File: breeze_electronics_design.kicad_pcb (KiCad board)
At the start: 2 copper layers, 104.1 x 104.1 mm, 107 parts, among them J1 SIP4, M1 MotorA, M2 MotorB, M3 MotorA, M4 MotorB, Q1 S8050, Q2 SI2302, Q3 SI2302, Q4 SI2302, Q5 SI2302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

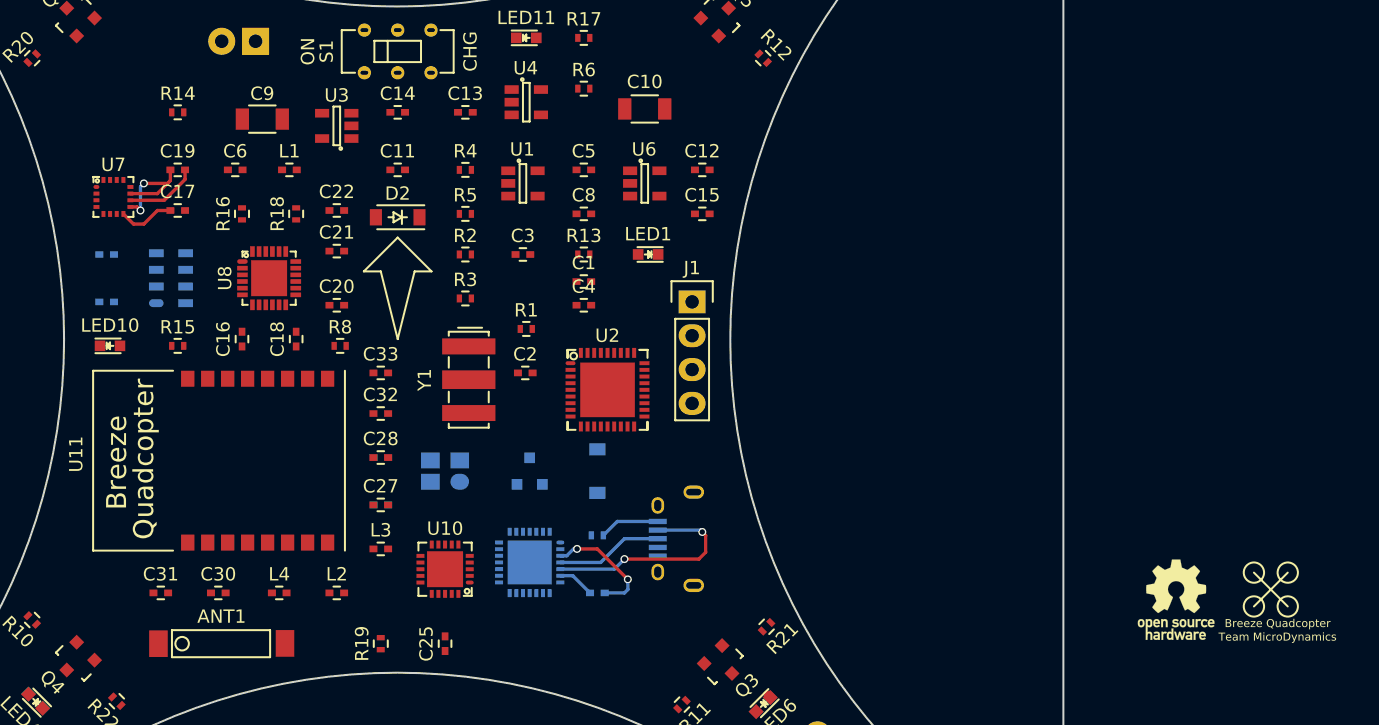
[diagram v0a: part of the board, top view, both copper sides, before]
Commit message: Adjust the layout of Sensor module
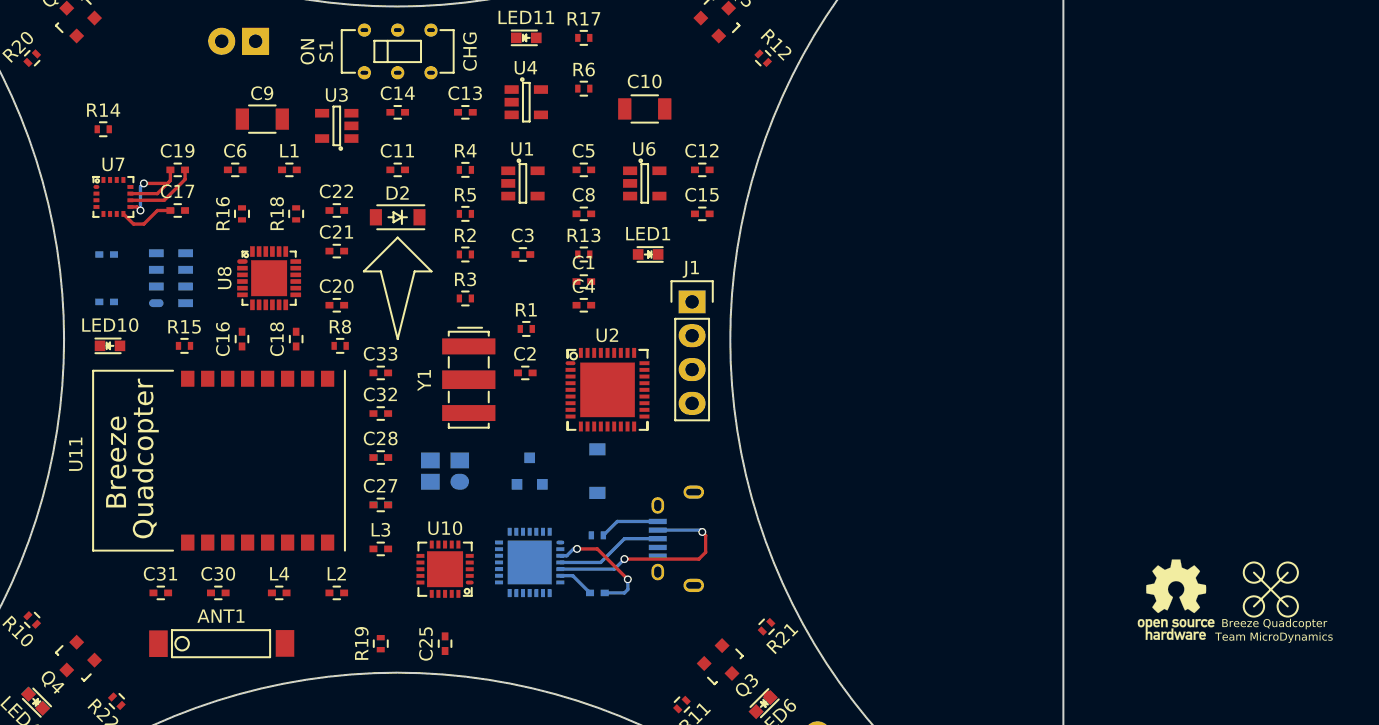
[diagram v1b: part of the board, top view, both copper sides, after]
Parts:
- REF**: footprint Footprint:LOGO_Project -> LOGO_Project
- moved R14 5.73 mm to (27.9, -65.8)
- moved R15 0.51 mm to (34.0, -49.5)
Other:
- net class Signal: clearance 0.2 -> 0.15
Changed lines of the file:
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@@
 (kicad_pcb (version 4) (host pcbnew 4.0.2+e4-6225~38~ubuntu14.04.1-stable)
   (general
-    (links 0)
+    (links 163)
     (no_connects 154)
-    (area -48.496 -119.575001 133.995 19.575001)
+    (area -19.575001 -119.575001 122.03062 19.575001)
     (thickness 1.6)
     (drawings 26)
@@
   )
   (net_class Signal ""
-    (clearance 0.2)
+    (clearance 0.15)
     (trace_width 0.25)
     (via_dia 0.6)
@@
     (add_net "Net-(Y1-Pad2)")
   )
+  (module LOGO_Project (layer F.Cu)
+    (at 115.57 -31.242)
+    (descr "Project logo")
+    (tags "Project logo")
+    (fp_text reference REF** (at 0.762 -1.524) (layer F.SilkS) hide
+      (effects (font (size 1 1) (thickness 0.15)))
+    )
+    (fp_text value LOGO_Project (at 0 0) (layer F.Fab) hide
+      (effects (font (size 1 1) (thickness 0.15)))
+    )
+    (fp_circle (center 1.27 1.27) (end 1.27 0.508) (layer F.SilkS) (width 0.15))
+    (fp_circle (center -1.27 1.27) (end -1.27 0.508) (layer F.SilkS) (width 0.15))
+    (fp_circle (center 1.27 -1.27) (end 1.27 -0.508) (layer F.SilkS) (width 0.15))
+    (fp_circle (center -1.27 -1.27) (end -1.27 -0.508) (layer F.SilkS) (width 0.15))
+    (fp_line (start 1.27 -1.27) (end -1.27 1.27) (layer F.SilkS) (width 0.15))
+    (fp_line (start -1.27 -1.27) (end 1.27 1.27) (layer F.SilkS) (width 0.15))
+    (fp_text user "Team MicroDynamics" (at 0.254 3.556) (layer F.SilkS)
+      (effects (font (size 0.6 0.6) (thickness 0.15)))
+    )
+    (fp_text user "Breeze Quadcopter" (at 0.254 2.54) (layer F.SilkS)
+      (effects (font (size 0.6 0.6) (thickness 0.15)))
+    )
+  )
   (module Footprint:QFN_CP2102 (layer B.Cu)
     (at 59.944 -33.274 180)
@@
   )
   (module Resistors_SMD:R_0402 (layer F.Cu)
-    (at 33.528 -67.056)
+    (at 27.94 -65.786)
     (descr "Resistor SMD 0402, reflow soldering, Vishay (see dcrcw.pdf)")
     (tags "resistor 0402")
@@
   )
   (module Resistors_SMD:R_0402 (layer F.Cu)
-    (at 33.528 -49.53 180)
+    (at 34.036 -49.53 180)
     (descr "Resistor SMD 0402, reflow soldering, Vishay (see dcrcw.pdf)")
     (tags "resistor 0402")
@@
       (net 192 "Net-(U11-Pad16)"))
   )
-  (module Footprint:LOGO_Project (layer F.Cu)
-    (at 115.57 -31.242)
-    (descr "Project logo")
-    (tags "Project logo")
-    (fp_text reference REF** (at 0.762 -1.524) (layer F.SilkS) hide
-      (effects (font (size 1 1) (thickness 0.15)))
-    )
-    (fp_text value LOGO_Project (at 0 0) (layer F.Fab) hide
-      (effects (font (size 1 1) (thickness 0.15)))
-    )
-    (fp_circle (center 1.27 1.27) (end 1.27 0.508) (layer F.SilkS) (width 0.15))
-    (fp_circle (center -1.27 1.27) (end -1.27 0.508) (layer F.SilkS) (width 0.15))
-    (fp_circle (center 1.27 -1.27) (end 1.27 -0.508) (layer F.SilkS) (width 0.15))
-    (fp_circle (center -1.27 -1.27) (end -1.27 -0.508) (layer F.SilkS) (width 0.15))
-    (fp_line (start 1.27 -1.27) (end -1.27 1.27) (layer F.SilkS) (width 0.15))
-    (fp_line (start -1.27 -1.27) (end 1.27 1.27) (layer F.SilkS) (width 0.15))
-    (fp_text user "Team MicroDynamics" (at 0.508 3.556) (layer F.SilkS)
-      (effects (font (size 0.6 0.6) (thickness 0.15)))
-    )
-    (fp_text user "Breeze Quadcopter" (at 0.508 2.54) (layer F.SilkS)
-      (effects (font (size 0.6 0.6) (thickness 0.15)))
-    )
-  )
   (gr_line (start 0 -100) (end 0 0) (angle 90) (layer Edge.Cuts) (width 0.15))

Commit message: Finish the major layout
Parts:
- C3, R2, R3: moved to B.Cu
- REF**: footprint Footprint:LOGO_Arrow -> LOGO_Arrow
- moved REF*** 49.1 mm to (59.4, -28.4)
- moved REF** 48.8 mm to (66.8, -29.2)
- moved R1 12.2 mm to (59.9, -38.6)
- moved C1 9.02 mm to (55.1, -55.9)
- moved C9 6.37 mm to (33.5, -66.0)
- moved C2 6.36 mm to (59.9, -41.1)
- moved Y1 5.89 mm to (54.6, -41.1)
- moved C4 5.64 mm to (59.4, -55.9)
- moved U2 4.88 mm to (62.0, -49.3)
- moved C6 4.17 mm to (40.4, -66.0)
- moved H1 3.84 mm to (35.6, -71.9)
- moved S1 2.55 mm to (47.5, -71.4)
- moved REF** 1.85 mm to (50.5, -53.3)
- moved R6 1.78 mm to (64.0, -67.1)
- moved L1 1.52 mm to (40.4, -62.7)
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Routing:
- net /DN: track 16.5 -> 0.00 mm, vias 2 -> 0
- net Net-(D2-Pad2): track 0.00 -> 12.7 mm
- net Net-(C19-Pad1): track 9.03 -> 0.00 mm, vias 2 -> 0
- net Net-(C7-Pad1): track 8.83 -> 0.00 mm, vias 2 -> 0
- net /DP: track 8.05 -> 0.00 mm
- net Net-(C6-Pad1): track 0.00 -> 5.65 mm
- net Net-(C19-Pad2): track 5.47 -> 0.00 mm
- net /VBUS: track 4.52 -> 0.00 mm
- net Net-(C17-Pad1): track 4.26 -> 0.00 mm
- net Net-(C11-Pad1): track 0.00 -> 4.01 mm
- net Net-(C7-Pad2): track 2.76 -> 0.00 mm
- net /I2C_SDA: track 0.00 -> 2.45 mm

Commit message: Move the PCB to the center of drawing
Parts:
- moved ? 173.2 mm to (100.8, 49.4)
- moved ? 173.2 mm to (190.7, 139.2)
- moved ? 173.2 mm to (190.7, 49.4)
- moved ? 173.2 mm to (100.8, 139.2)
- moved ANT1 173.2 mm to (132.6, 117.1)
- moved C1 173.2 mm to (150.9, 88.4)
- moved C10 173.2 mm to (164.3, 76.5)
- moved C11 173.2 mm to (146.3, 81.5)
- moved C12 173.2 mm to (168.4, 81.5)
- moved C13 173.2 mm to (150.9, 78.2)
- moved C14 173.2 mm to (146.3, 78.2)
- moved C15 173.2 mm to (168.4, 85.1)
- moved C16 173.2 mm to (134.1, 94.2)
- moved C17 173.2 mm to (129.3, 84.8)
- moved C18 173.2 mm to (138.2, 94.2)
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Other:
- outline, holes or cut-outs redrawn

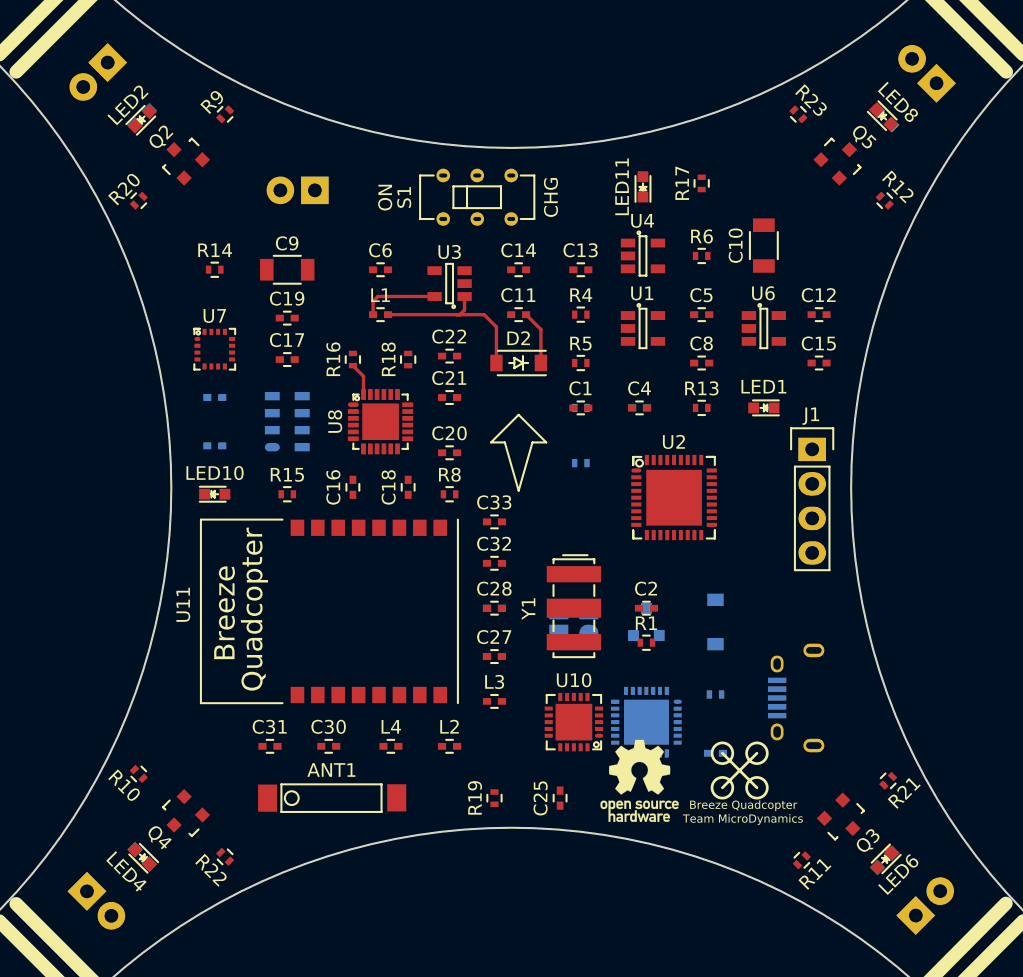
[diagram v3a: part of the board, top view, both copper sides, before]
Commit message: Finish the automatic routing of Motors
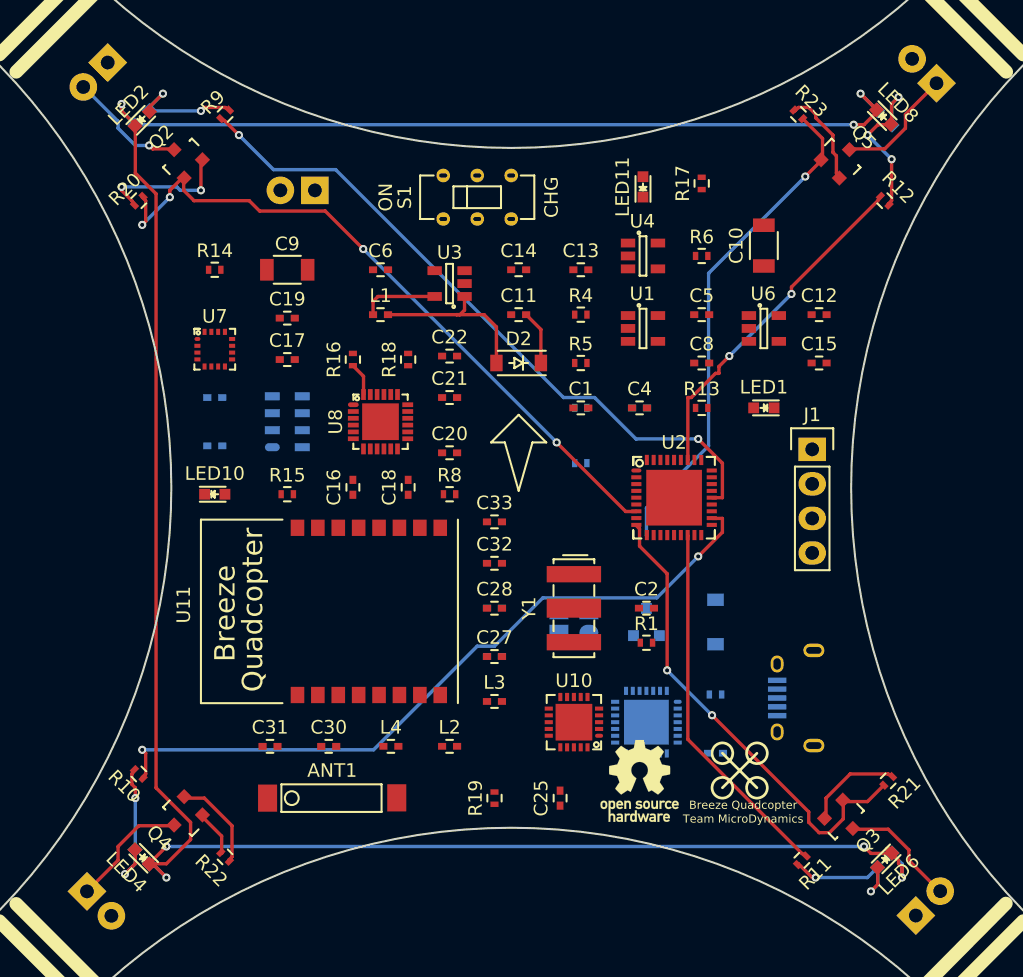
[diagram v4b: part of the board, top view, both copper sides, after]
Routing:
- net Net-(LED2-Pad1): track 0.40 -> 184.5 mm, vias 0 -> 7
- net /PA8: track 0.00 -> 53.4 mm, vias 0 -> 2
- net /PWMA: track 0.00 -> 51.5 mm, vias 0 -> 4
- net /PA11: track 0.00 -> 50.7 mm, vias 0 -> 2
- net /PWMD: track 0.00 -> 36.9 mm, vias 0 -> 1
- net /PWMC: track 0.00 -> 35.4 mm, vias 0 -> 2
- net /PB1: track 0.00 -> 27.3 mm
- net /PB3: track 0.00 -> 25.5 mm, vias 0 -> 2
- net Net-(LED8-Pad2): track 0.00 -> 12.7 mm, vias 0 -> 3
- net Net-(LED6-Pad2): track 0.00 -> 10.7 mm, vias 0 -> 2
- net Net-(LED4-Pad2): track 0.00 -> 10.3 mm, vias 0 -> 2
- net Net-(Q2-Pad2): track 0.00 -> 10.1 mm, vias 0 -> 2
- net Net-(LED2-Pad2): track 0.03 -> 9.60 mm, vias 0 -> 2
- net Net-(M4-Pad1): track 0.00 -> 9.02 mm
- net Net-(M2-Pad1): track 0.00 -> 9.02 mm
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
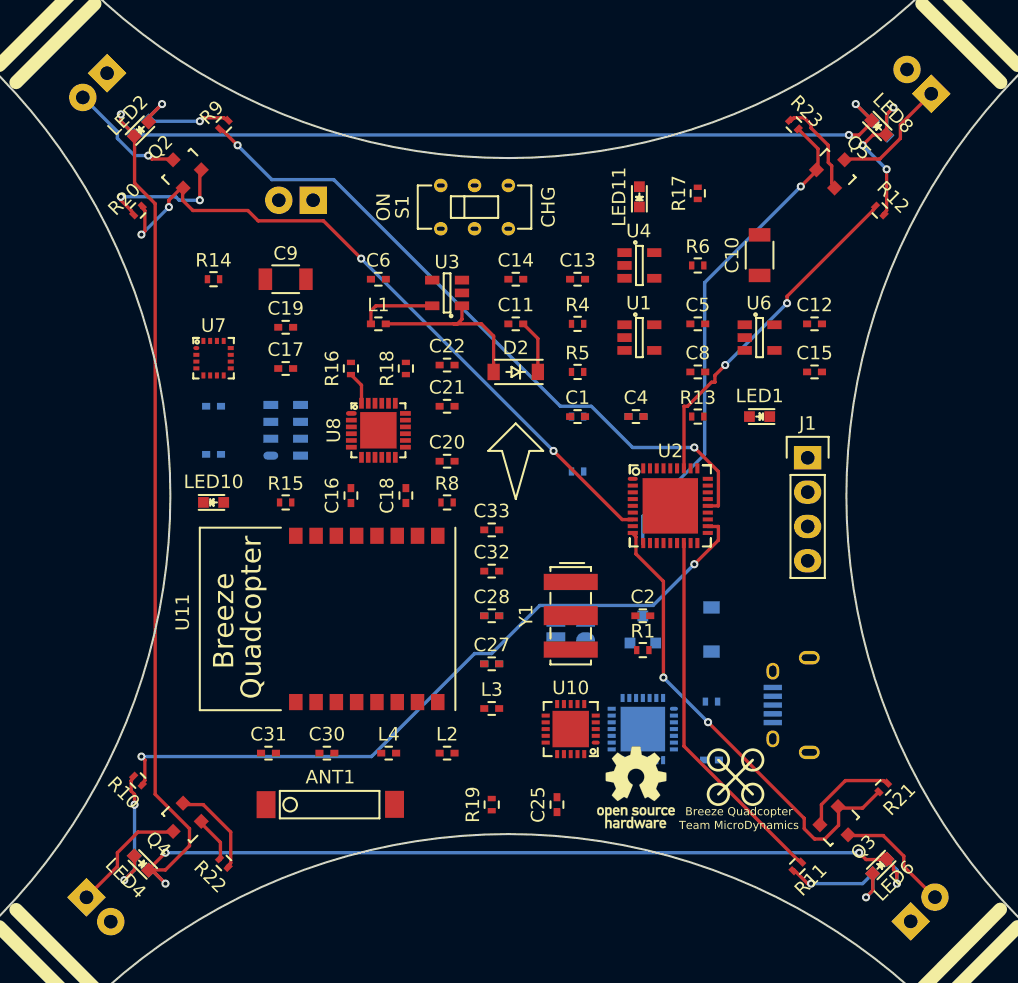
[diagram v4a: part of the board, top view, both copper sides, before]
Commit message: Finish the wiring of Motors
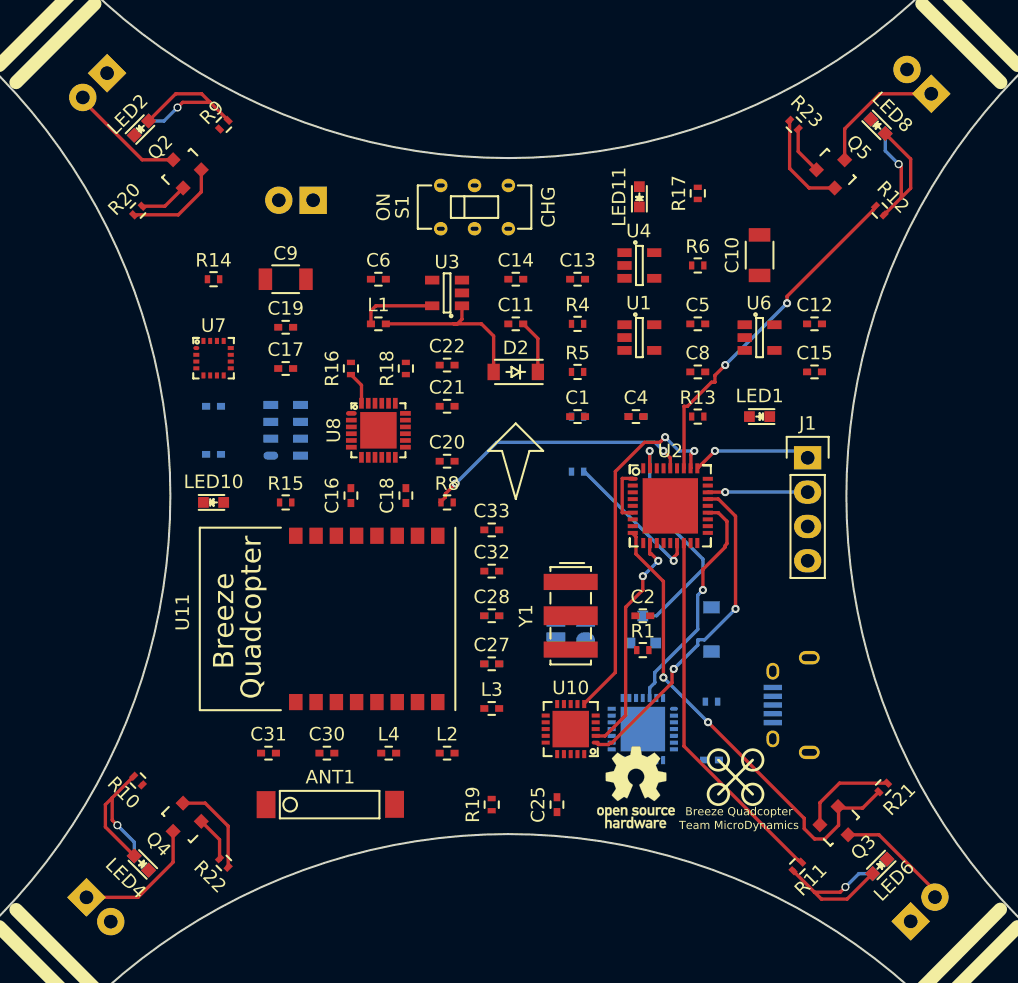
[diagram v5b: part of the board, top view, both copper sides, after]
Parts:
- moved LED9 0.18 mm to (173.1, 66.9)
- moved LED8 0.09 mm to (173.1, 66.9)
- moved LED2 0.08 mm to (118.6, 67.1)
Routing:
- net Net-(LED2-Pad1): track 184.5 -> 0.00 mm, vias 7 -> 0
- net /PA8: track 53.4 -> 0.12 mm, vias 2 -> 0
- net /PA11: track 50.7 -> 0.00 mm, vias 2 -> 0
- net /PWMA: track 51.5 -> 3.92 mm, vias 4 -> 0
- net /PWMD: track 36.9 -> 3.81 mm, vias 1 -> 0
- net /NRF_IRQ: track 0.00 -> 26.9 mm, vias 0 -> 2
- net /CE: track 0.00 -> 24.7 mm, vias 0 -> 2
- net /MP_INT: track 0.00 -> 20.3 mm, vias 0 -> 2
- net /BOOT0: track 0.00 -> 17.6 mm, vias 0 -> 1
- net /RXD_BT: track 0.00 -> 17.1 mm, vias 0 -> 1
- net /CSN: track 0.00 -> 16.9 mm, vias 0 -> 2
- net /BAT_DET: track 0.00 -> 10.8 mm, vias 0 -> 1
- net /SWCLK: track 0.00 -> 8.90 mm, vias 0 -> 1
- net /SWDIO: track 0.00 -> 7.39 mm, vias 0 -> 1
- net Net-(U2-Pad1): track 0.00 -> 4.12 mm
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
